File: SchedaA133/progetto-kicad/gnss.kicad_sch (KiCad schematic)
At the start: 26 parts, among them J701 SMA antenna, J702 SMA PPS OUT, J703 SMA STROBE IN, J704 PPS/STROBE, U701 NEO-F10T, U702 74LVC1G17, U703 74LVC1G17

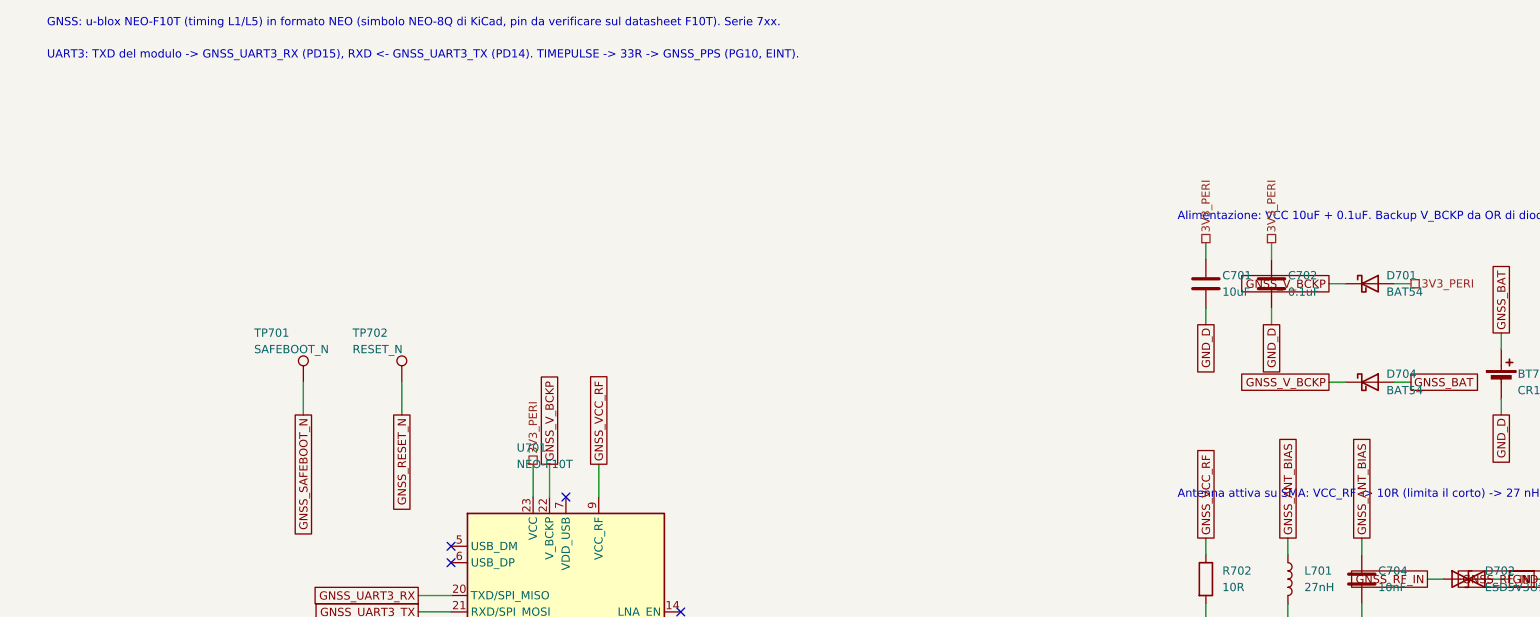
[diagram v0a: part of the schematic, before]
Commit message: SchedaA133: NEO-F10T sostituito dal NEO-M9N-00B
- Simbolo RF_GPS:NEO-M9N, pin verificati sul data sheet UBX-19014285 R08 (tabella 9)
- Collegamenti invariati sui pin comuni; V_USB (pin 7) ora a GND, D_SEL, USB, LNA_EN, SDA/SCL liberi
- README, bom-a133.csv (U10) e documenti aggiornati, eMMC resta 256 GB
- ERC 0, schema-a133.pdf riesportato

Co-Authored-By: Claude Opus 5.5 (1M context) <noreply@anthropic.com>
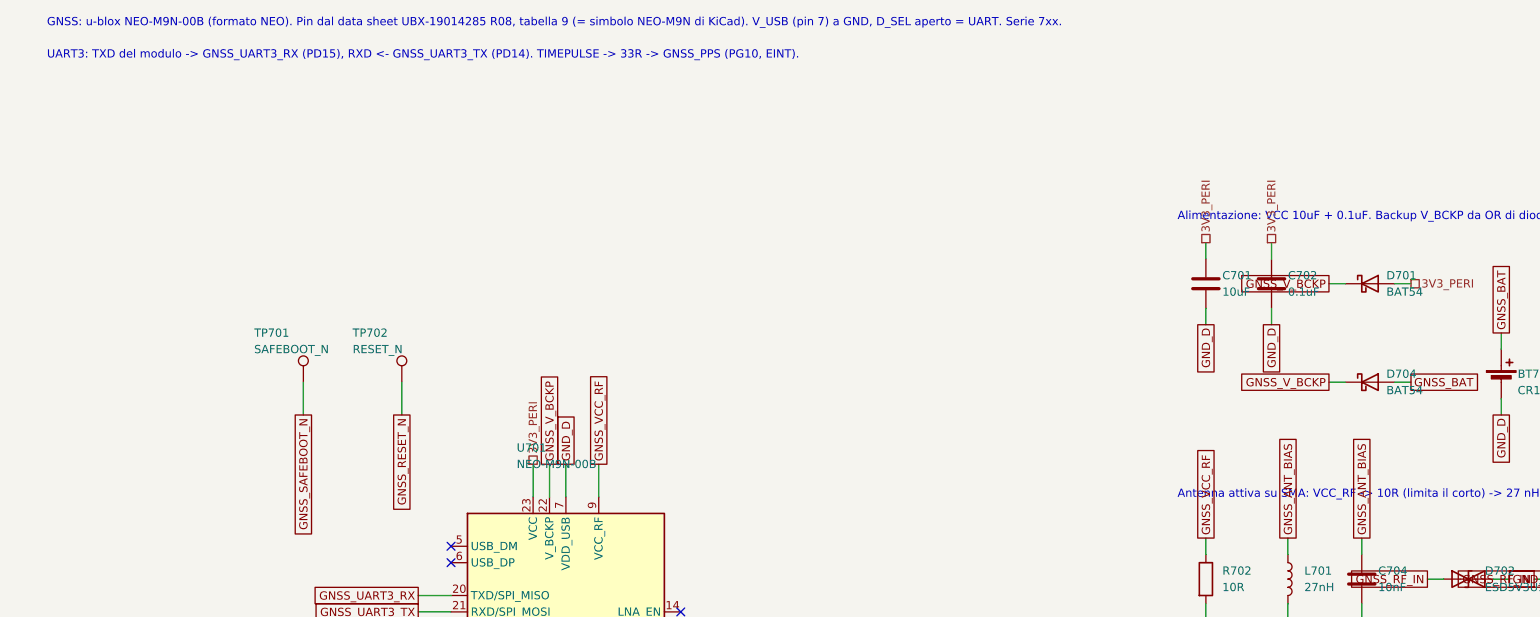
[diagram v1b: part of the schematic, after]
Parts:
- U701: value NEO-F10T -> NEO-M9N-00B; symbol RF_GPS:NEO-8Q -> RF_GPS:NEO-M9N; MPN NEO-F10T -> NEO-M9N-00B
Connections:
- net GND_D: now also U701.7 (VDD_USB)
- no-connect marks 12 -> 11
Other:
- note added: "GNSS: u-blox NEO-M9N-00B (formato NEO). Pin dal data sheet UBX-19014285 R08, tabella 9 (= simbolo NEO-M9N di KiCad). V_USB (pin 7) a GND, D_SEL aperto = UART. Serie 7xx."
- note removed: "GNSS: u-blox NEO-F10T (timing L1/L5) in formato NEO (simbolo NEO-8Q di KiCad, pin da verificare sul datasheet F10T). Serie 7xx."
